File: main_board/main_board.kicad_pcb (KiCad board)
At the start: 2 copper layers, 26 x 53 mm, 6 parts, among them J1 Conn_01x16, U1 Pico, U2 MPR121QR2

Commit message: Alignment fixes, generate gerbers
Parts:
- moved U1 0.08 mm to (123.0, 64.3)
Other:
- board text added: "clue & dj505"

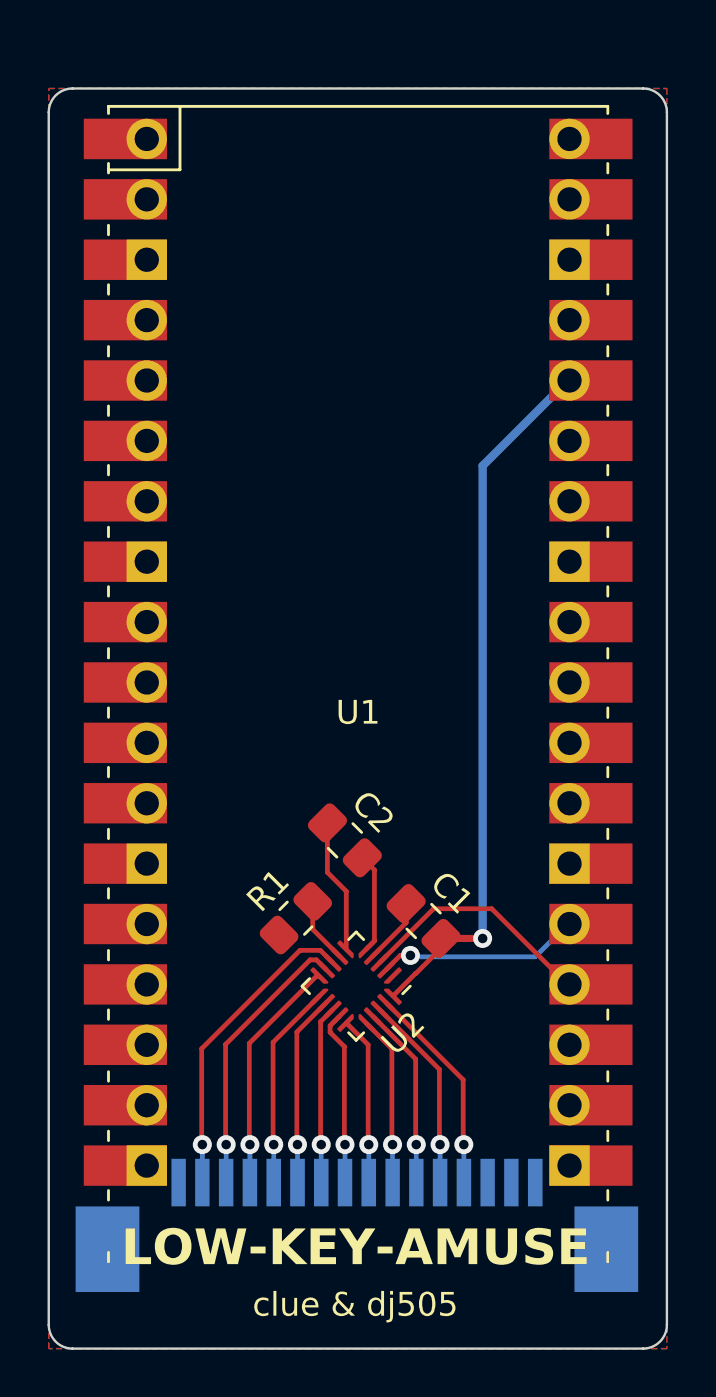
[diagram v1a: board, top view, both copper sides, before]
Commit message: Add tooling holes, update logo, other adjustments
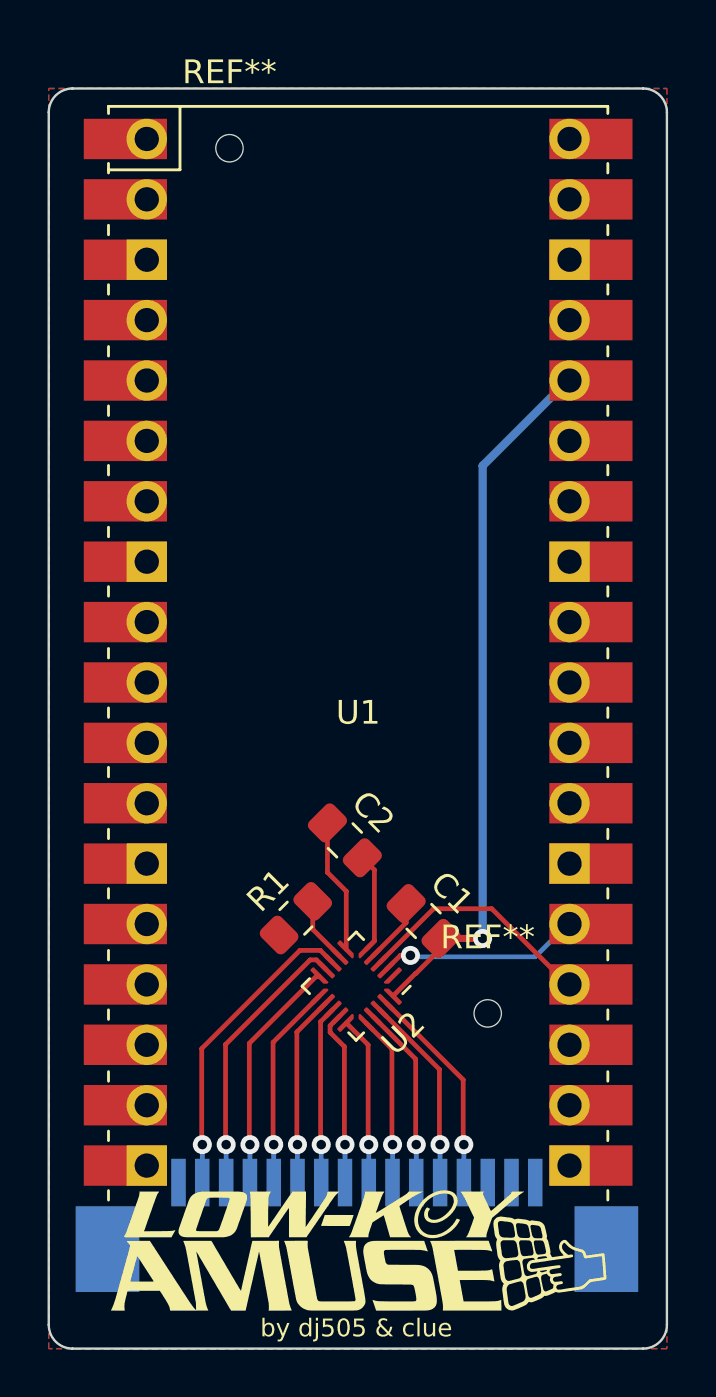
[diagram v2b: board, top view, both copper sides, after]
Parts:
- added G***: LOGO, low-key-amuse:logo_small, F.Cu at (123.0, 86.9)
- added G***: LOGO, low-key-amuse:logo_medium, B.Cu at (122.9, 60.2)
- added REF**: MountingHole_2.1mm, MountingHole:MountingHole_2.1mm, F.Cu at (117.6, 40.5)
- added REF**: MountingHole_2.1mm, MountingHole:MountingHole_2.1mm, F.Cu at (128.5, 76.9)
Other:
- board text added: "by dj505 & clue"
- board text removed: "LOW-KEY-AMUSE"
- board text removed: "clue & dj505"
